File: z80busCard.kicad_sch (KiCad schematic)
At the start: 10 parts, among them J1 Conn_02x20_Odd_Even, J2 Conn_02x20_Odd_Even, J3 Conn_02x20_Odd_Even, J4 Conn_02x20_Odd_Even, J5 USB_C_Receptacle_PowerOnly_6P, SW1 SW_Push

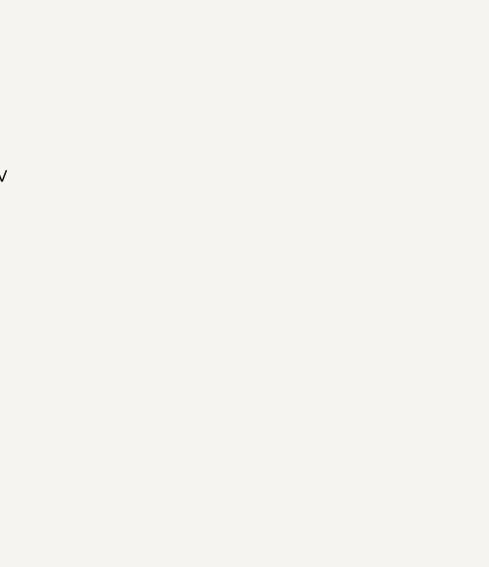
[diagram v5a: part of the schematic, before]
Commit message: Added power diode
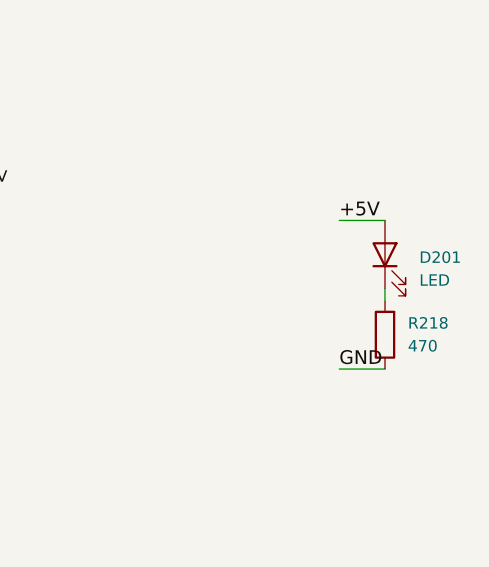
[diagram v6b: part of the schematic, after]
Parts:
- added D201: LED, LED_SMD:LED_0805_2012Metric_Pad1.15x1.40mm_HandSolder, symbol Device:LED
- added R218: 470, Resistor_SMD:R_0805_2012Metric_Pad1.20x1.40mm_HandSolder, symbol Device:R
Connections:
- net +5V: now also D201.2 (A)
- net GND: now also R218.1
- new net: D201.1 (K), R218.2
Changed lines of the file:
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@@
 	(wire
 		(pts
+			(xy 242.57 120.65) (xy 247.65 120.65)
+		)
+		(stroke
+			(width 0)
+			(type default)
+		)
+	)
+	(wire
+		(pts
 			(xy 184.15 90.17) (xy 186.69 90.17)
 		)
@@
 	(wire
 		(pts
+			(xy 242.57 137.16) (xy 247.65 137.16)
+		)
+		(stroke
+			(width 0)
+			(type default)
+		)
+	)
+	(wire
+		(pts
 			(xy 49.53 96.52) (xy 58.42 96.52)
 		)
@@
 	(wire
 		(pts
+			(xy 247.65 128.27) (xy 247.65 129.54)
+		)
+		(stroke
+			(width 0)
+			(type default)
+		)
+	)
+	(wire
+		(pts
 			(xy 124.46 99.06) (xy 133.35 99.06)
 		)
@@
 		)
 	)
+	(label "GND"
+		(at 242.57 137.16 0)
+		(effects
+			(font
+				(size 1.524 1.524)
+			)
+			(justify left bottom)
+		)
+	)
 	(label "~{M1}"
 		(at 124.46 68.58 0)
@@
 		)
 	)
+	(label "+5V"
+		(at 242.57 120.65 0)
+		(effects
+			(font
+				(size 1.524 1.524)
+			)
+			(justify left bottom)
+		)
+	)
 	(label "D1"
 		(at 148.59 58.42 0)
@@
 	(symbol
 		(lib_id "Device:R")
+		(at 247.65 133.35 180)
+		(unit 1)
+		(exclude_from_sim no)
+		(in_bom yes)
+		(on_board yes)
+		(dnp no)
+		(fields_autoplaced yes)
+		(property "Reference" "R218"
+			(at 250.19 132.0799 0)
+			(effects
+				(font
+					(size 1.27 1.27)
+				)
+				(justify right)
+			)
+		)
+		(property "Value" "470"
+			(at 250.19 134.6199 0)
+			(effects
+				(font
+					(size 1.27 1.27)
+				)
+				(justify right)
+			)
+		)
+		(property "Footprint" "Resistor_SMD:R_0805_2012Metric_Pad1.20x1.40mm_HandSolder"
+			(at 249.428 133.35 90)
+			(effects
+				(font
+					(size 1.27 1.27)
+				)
+				(hide yes)
+			)
+		)
+		(property "Datasheet" "~"
+			(at 247.65 133.35 0)
+			(effects
+				(font
+					(size 1.27 1.27)
+				)
+				(hide yes)
+			)
+		)
+		(property "Description" "Resistor"
+			(at 247.65 133.35 0)
+			(effects
+				(font
+					(size 1.27 1.27)
+				)
+				(hide yes)
+			)
+		)
+		(pin "2"
+		)
+		(pin "1"
+		)
+		(instances
+			(project "z80busCard"
+				(path "/38e6c7dd-e4e5-4fac-a332-e7467610bd5b"
+					(reference "R218")
+					(unit 1)
+				)
+			)
+		)
+	)
+	(symbol
+		(lib_id "Device:R")
 		(at 198.12 128.27 0)
 		(unit 1)
@@
 					(unit 1)
 				)
+			)
+		)
+	)
+	(symbol
+		(lib_id "Device:LED")
+		(at 247.65 124.46 90)
+		(unit 1)
+		(exclude_from_sim no)
+		(in_bom yes)
+		(on_board yes)
+		(dnp no)
+		(fields_autoplaced yes)
+		(property "Reference" "D201"
+			(at 251.46 124.7774 90)
+			(effects
+				(font
+					(size 1.27 1.27)
+				)
+				(justify right)
+			)
+		)
+		(property "Value" "LED"
+			(at 251.46 127.3174 90)
+			(effects
+				(font
+					(size 1.27 1.27)
+				)
+				(justify right)
+			)
+		)
+		(property "Footprint" "LED_SMD:LED_0805_2012Metric_Pad1.15x1.40mm_HandSolder"
+			(at 247.65 124.46 0)
+			(effects
+				(font
+					(size 1.27 1.27)
+				)
+				(hide yes)
+			)
+		)
+		(property "Datasheet" "~"
+			(at 247.65 124.46 0)
+			(effects
+				(font
+					(size 1.27 1.27)
+				)
+				(hide yes)
+			)
+		)
+		(property "Description" "Light emitting diode"
+			(at 247.65 124.46 0)
+			(effects
+				(font
+					(size 1.27 1.27)
+				)
+				(hide yes)
+			)
+		)
+		(property "Sim.Pins" "1=K 2=A"
+			(at 247.65 124.46 0)
+			(effects
+				(font
+					(size 1.27 1.27)
+				)
+				(hide yes)
+			)
+		)
+		(pin "2"
+		)
+		(pin "1"
+		)
+		(instances
+			(project "z80busCard"
+				(path "/38e6c7dd-e4e5-4fac-a332-e7467610bd5b"
+					(reference "D201")
+					(unit 1)
+				)

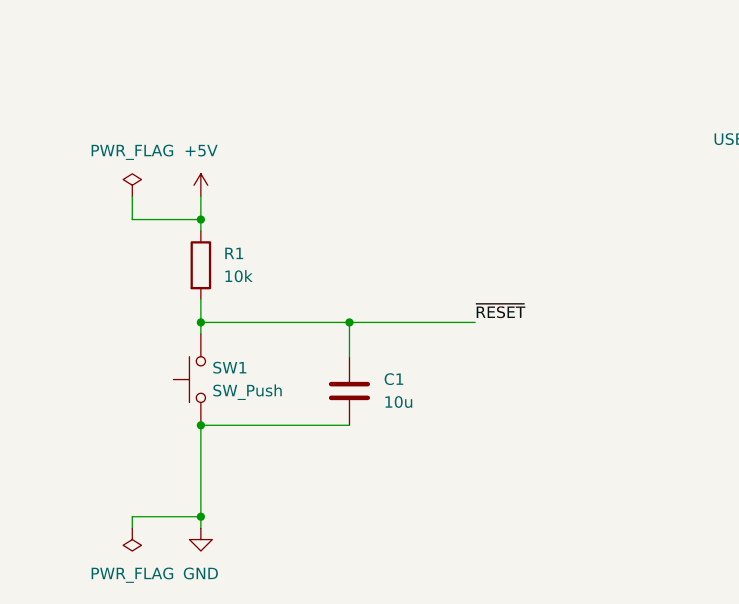
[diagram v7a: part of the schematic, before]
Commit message: Replaced Mounting Hole with Mounting hole pad
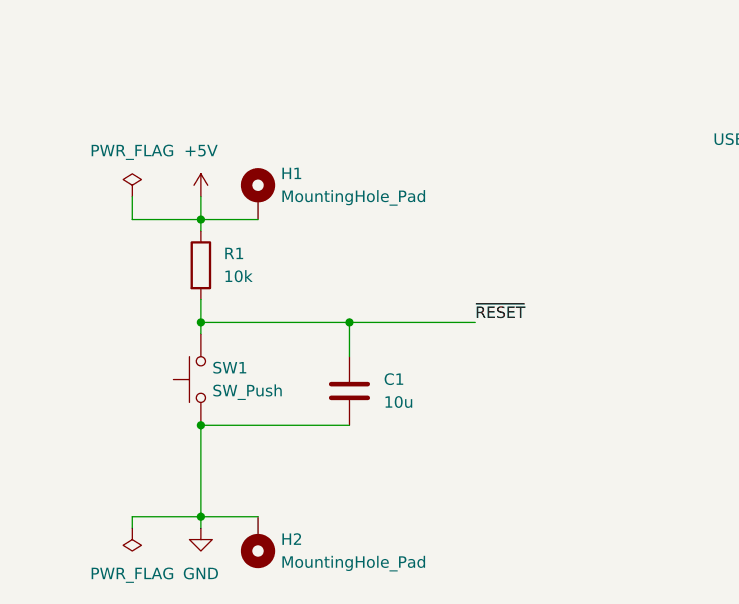
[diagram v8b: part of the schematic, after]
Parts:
- added H1, H2: MountingHole_Pad, MountingHole:MountingHole_4.3mm_M4_ISO14580_Pad_TopBottom, symbol Mechanical:MountingHole_Pad
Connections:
- net +5V: now also H1.1
- net GND: now also H2.1
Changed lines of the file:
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@@
 	(wire
 		(pts
+			(xy 69.85 149.86) (xy 76.2 149.86)
+		)
+		(stroke
+			(width 0)
+			(type default)
+		)
+	)
+	(wire
+		(pts
 			(xy 187.96 139.7) (xy 194.31 139.7)
 		)
@@
 	(wire
 		(pts
+			(xy 69.85 182.88) (xy 76.2 182.88)
+		)
+		(stroke
+			(width 0)
+			(type default)
+		)
+	)
+	(wire
+		(pts
 			(xy 146.05 88.9) (xy 148.59 88.9)
 		)
@@
 	)
 	(symbol
+		(lib_id "Mechanical:MountingHole_Pad")
+		(at 76.2 185.42 180)
+		(unit 1)
+		(body_style 1)
+		(exclude_from_sim no)
+		(in_bom no)
+		(on_board yes)
+		(in_pos_files yes)
+		(dnp no)
+		(property "Reference" "H2"
+			(at 78.74 185.4199 0)
+			(show_name no)
+			(do_not_autoplace no)
+			(effects
+				(font
+					(size 1.27 1.27)
+				)
+				(justify right)
+			)
+		)
+		(property "Value" "MountingHole_Pad"
+			(at 78.74 187.9599 0)
+			(show_name no)
+			(do_not_autoplace no)
+			(effects
+				(font
+					(size 1.27 1.27)
+				)
+				(justify right)
+			)
+		)
+		(property "Footprint" "MountingHole:MountingHole_4.3mm_M4_ISO14580_Pad_TopBottom"
+			(at 76.2 185.42 0)
+			(hide yes)
+			(show_name no)
+			(do_not_autoplace no)
+			(effects
+				(font
+					(size 1.27 1.27)
+				)
+			)
+		)
+		(property "Datasheet" ""
+			(at 76.2 185.42 0)
+			(hide yes)
+			(show_name no)
+			(do_not_autoplace no)
+			(effects
+				(font
+					(size 1.27 1.27)
+				)
+			)
+		)
+		(property "Description" "Mounting Hole with connection"
+			(at 76.2 185.42 0)
+			(hide yes)
+			(show_name no)
+			(do_not_autoplace no)
+			(effects
+				(font
+					(size 1.27 1.27)
+				)
+			)
+		)
+		(pin "1"
+		)
+		(instances
+			(project "z80busCard"
+				(path "/38e6c7dd-e4e5-4fac-a332-e7467610bd5b"
+					(reference "H2")
+					(unit 1)
+				)
+			)
+		)
+	)
+	(symbol
 		(lib_id "power:PWR_FLAG")
 		(at 62.23 184.15 180)
@@
 					(unit 1)
 				)
+			)
+		)
+	)
+	(symbol
+		(lib_id "Mechanical:MountingHole_Pad")
+		(at 76.2 147.32 0)
+		(unit 1)
+		(body_style 1)
+		(exclude_from_sim no)
+		(in_bom no)
+		(on_board yes)
+		(in_pos_files yes)
+		(dnp no)
+		(fields_autoplaced yes)
+		(property "Reference" "H1"
+			(at 78.74 144.7799 0)
+			(show_name no)
+			(do_not_autoplace no)
+			(effects
+				(font
+					(size 1.27 1.27)
+				)
+				(justify left)
+			)
+		)
+		(property "Value" "MountingHole_Pad"
+			(at 78.74 147.3199 0)
+			(show_name no)
+			(do_not_autoplace no)
+			(effects
+				(font
+					(size 1.27 1.27)
+				)
+				(justify left)
+			)
+		)
+		(property "Footprint" "MountingHole:MountingHole_4.3mm_M4_ISO14580_Pad_TopBottom"
+			(at 76.2 147.32 0)
+			(hide yes)
+			(show_name no)
+			(do_not_autoplace no)
+			(effects
+				(font
+					(size 1.27 1.27)
+				)
+			)
+		)
+		(property "Datasheet" ""
+			(at 76.2 147.32 0)
+			(hide yes)
+			(show_name no)
+			(do_not_autoplace no)
+			(effects
+				(font
+					(size 1.27 1.27)
+				)
+			)
+		)
+		(property "Description" "Mounting Hole with connection"
+			(at 76.2 147.32 0)
+			(hide yes)
+			(show_name no)
+			(do_not_autoplace no)
+			(effects
+				(font
+					(size 1.27 1.27)
+				)
+			)
+		)
+		(pin "1"
+		)
+		(instances
+			(project "z80busCard"
+				(path "/38e6c7dd-e4e5-4fac-a332-e7467610bd5b"
+					(reference "H1")
+					(unit 1)
+				)
